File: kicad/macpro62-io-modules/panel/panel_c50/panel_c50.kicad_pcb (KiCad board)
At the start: 2 copper layers, 97.2 x 97.8 mm, 55 parts, among them J1_C1 MOD-C - HOAUC HYCW417-USBC24-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, J1_C2 MOD-C - HOAUC HYCW417-USBC24-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, J1_C3 MOD-C - HOAUC HYCW417-USBC24-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, J1_C4 MOD-C - HOAUC HYCW417-USBC24-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, J1_C5 MOD-C - HOAUC HYCW417-USBC24-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, J1_C6 MOD-C - HOAUC HYCW417-USBC24-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, J1_H MOD-H - HOAUC HYC79-HDMIA19-1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, J2_C1 DF40C-50DP-0.4V(51) C424645 -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, J2_C2 DF40C-50DP-0.4V(51) C424645 -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, J2_C3 DF40C-50DP-0.4V(51) C424645 -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, J2_C4 DF40C-50DP-0.4V(51) C424645 -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, J2_C5 DF40C-50DP-0.4V(51) C424645 -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, J2_C6 DF40C-50DP-0.4V(51) C424645 -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, J2_H DF40C-50DP-0.4V(51) C424645 -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, U1_C1 BL24C02F-NTRC (C2828222) 24C0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, U1_C2 BL24C02F-NTRC (C2828222) 24C0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, U1_C3 BL24C02F-NTRC (C2828222) 24C0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, U1_C4 BL24C02F-NTRC (C2828222) 24C0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, U1_C5 BL24C02F-NTRC (C2828222) 24C0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, U1_C6 BL24C02F-NTRC (C2828222) 24C0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, U1_H BL24C02F-NTRC (C2828222) 24C0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

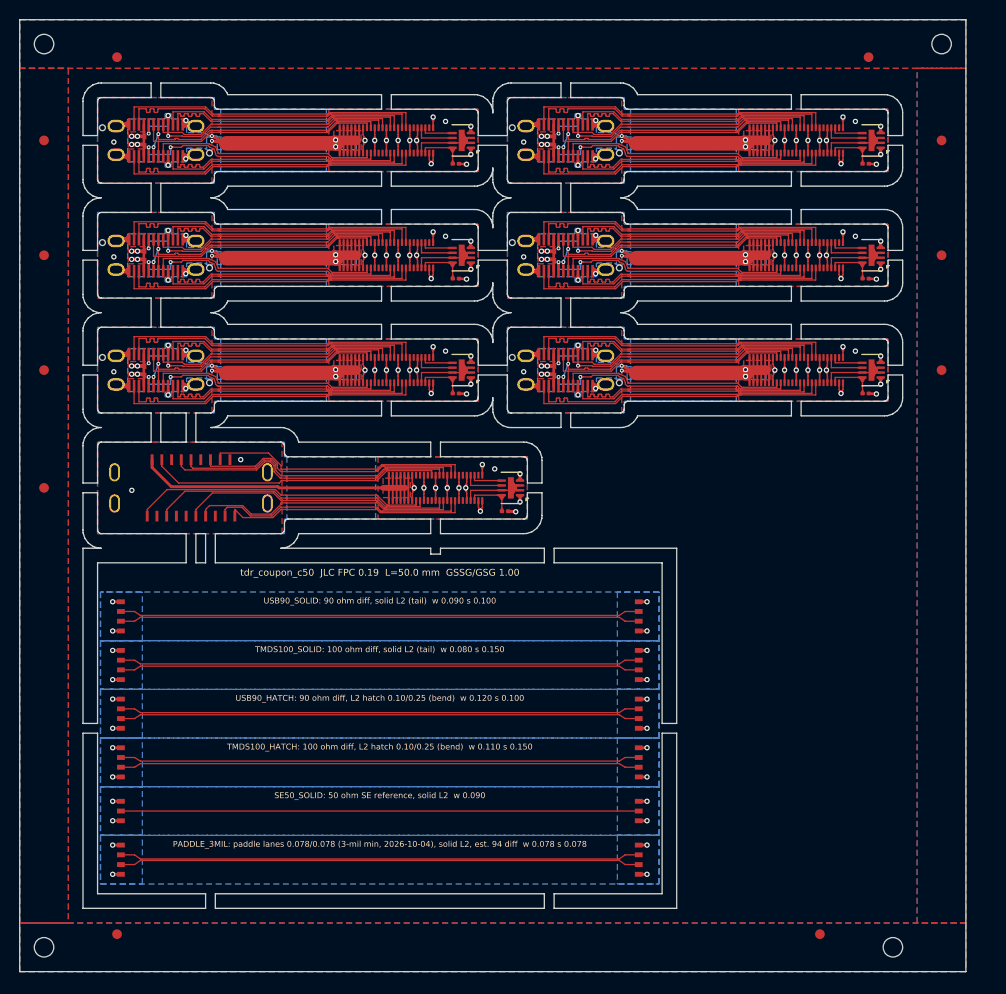
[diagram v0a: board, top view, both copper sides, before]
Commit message: Plate test-print fixes (corners +1mm Y, C2 post -1mm, C1 removed); USB-A/HDMI hand fan-out 0 skew; real DF40 + HDMI footprints
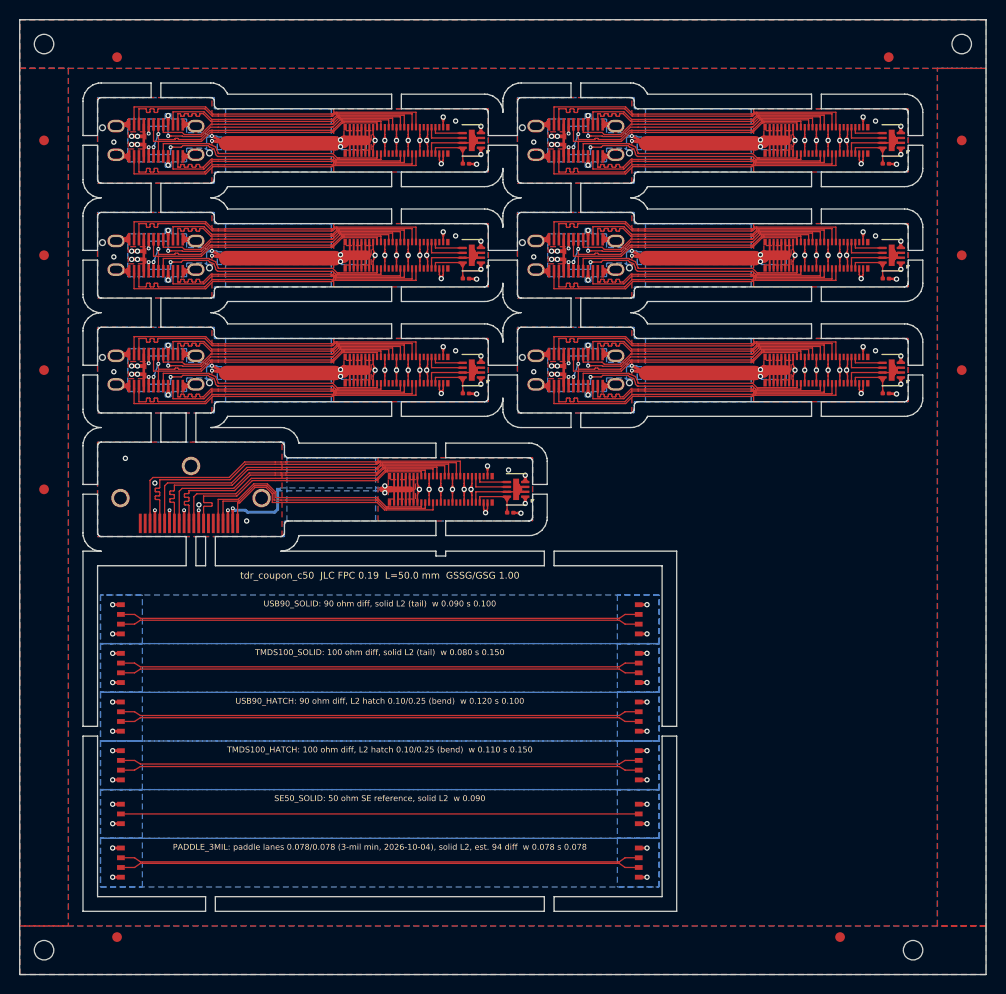
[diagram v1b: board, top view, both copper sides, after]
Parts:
- removed the J1_H at (17.6, 48.1)
- removed the J2_H at (42.7, 48.1)
- added J1_H: MOD-H - HOAUC HYC79-HDMIA19-105 (C711353) 19 SMD (1 row, 0.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, MP62_MOD:HOAUC_HYC79-HDMIA19-105, F.Cu at (17.6, 48.3)
- added J2_H: DF40C-50DP-0.4V(51) C424645 -> JMn DF40C-50DS (PMI-50 v2), MP62_MOD:MP62_Hirose_DF40C-50DP-0.4V, F.Cu at (43.3, 48.3)
- J2_C1, J2_C2, J2_C3, J2_C4, J2_C5, J2_C6: footprint MP62_MOD:MP62_Hirose_DF40C-50DP-0.4V_PLACEHOLDER -> MP62_MOD:MP62_Hirose_DF40C-50DP-0.4V
- moved FID4 2.09 mm to (84.3, 94.2)
- moved TH4 2.09 mm to (91.8, 95.6)
- moved J2_C2 2.07 mm to (81.9, 12.4)
- moved J2_C4 2.07 mm to (81.9, 24.2)
- moved J2_C6 2.07 mm to (81.9, 36.0)
- moved C1_C2 2.07 mm to (89.0, 14.8)
- moved C1_C4 2.07 mm to (89.0, 26.6)
- moved C1_C6 2.07 mm to (89.0, 38.4)
- moved U1_C2 2.07 mm to (89.6, 12.4)
- moved U1_C4 2.07 mm to (89.6, 24.2)
- moved U1_C6 2.07 mm to (89.6, 36.0)
- moved FID10 2.07 mm to (96.8, 36.0)
- moved FID2 2.07 mm to (89.3, 3.85)
- moved FID6 2.07 mm to (96.8, 12.4)
- moved FID8 2.07 mm to (96.8, 24.2)
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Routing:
- net H/VBUS: track 43.6 -> 28.2 mm, vias 0 -> 3
- net H/D2_P: track 25.4 -> 38.7 mm
- net H/D2_N: track 26.0 -> 38.7 mm
- net H/D1_P: track 27.0 -> 35.2 mm
- net H/D1_N: track 27.7 -> 35.2 mm
- net H/GND: track 28.3 -> 35.6 mm, vias 14 -> 21
- net H/HPD: track 30.3 -> 25.1 mm
- net H/DDC_SDA: track 30.2 -> 25.7 mm
- net H/D0_P: track 27.4 -> 31.7 mm
- net H/D0_N: track 27.8 -> 31.7 mm
- net H/DDC_SCL: track 28.8 -> 25.8 mm
- net H/CK_N: track 29.8 -> 28.3 mm
- net C5/D_P: track 26.5 -> 27.5 mm
- net C6/SSTX1_P: track 31.7 -> 32.7 mm
- net C6/D_P: track 26.5 -> 27.5 mm
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- added copper zone on B.Cu, net H/VBUS
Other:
- board size 97.2 x 97.8 mm -> 99.3 x 98.1 mm
- board text added: "panel_c50 C1 C2 C3 C4 C5 C6 H T 99.3 x 98.1 mm (JLC FPC 2L 12 um Cu ENIG, coverlay both sides, FR4 stiffeners per User.1)"
- board text removed: "panel_c50 C1 C2 C3 C4 C5 C6 H T 97.2 x 97.8 mm (JLC FPC 2L 12 um Cu ENIG, coverlay both sides, FR4 stiffeners per User.1)"
